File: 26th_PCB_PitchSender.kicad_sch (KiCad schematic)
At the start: 15 parts, among them J1 Amp, J2 Conn_01x04_Pin, J3 microSD, J4 Conn_01x04_Socket, J5 BNO055, J6 BMP390

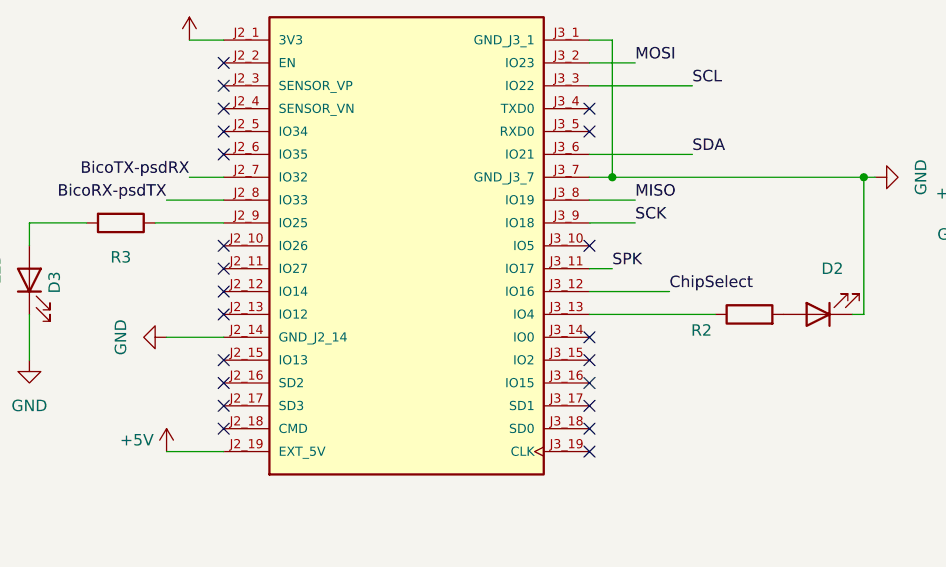
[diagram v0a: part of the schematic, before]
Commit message: Change SPK pin
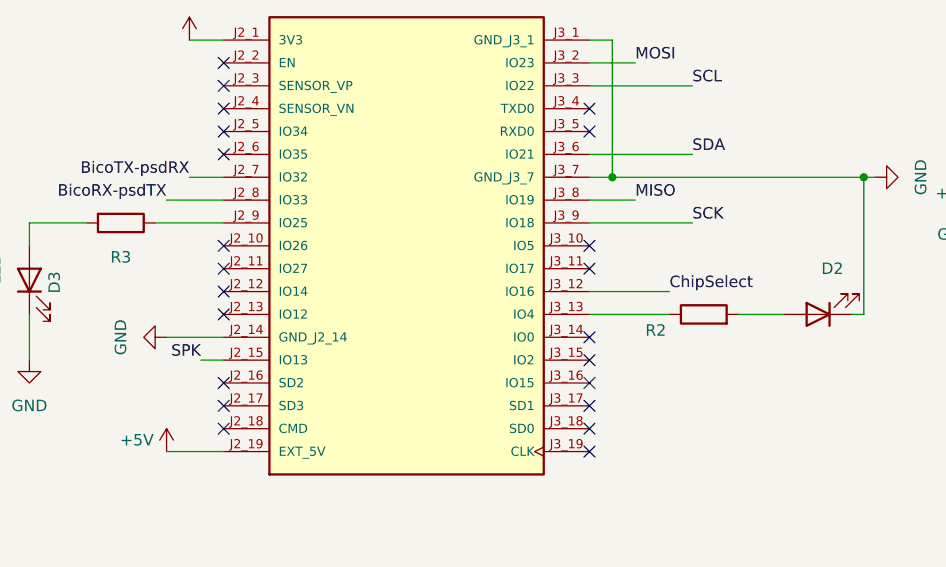
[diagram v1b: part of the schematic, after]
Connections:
- net SPK: now also U1.J2_15 (IO13); no longer U1.J3_11 (IO17)
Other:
- moved on the sheet: R2
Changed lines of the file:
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@@
 	)
 	(no_connect
-		(at 144.78 129.54)
-	)
-	(no_connect
 		(at 144.78 137.16)
 	)
@@
 	)
 	(no_connect
+		(at 185.42 119.38)
+	)
+	(no_connect
 		(at 144.78 121.92)
 	)
@@
 	(wire
 		(pts
-			(xy 185.42 119.38) (xy 187.96 119.38)
+			(xy 229.87 114.3) (xy 236.22 114.3)
 		)
 		(stroke
@@
 	(wire
 		(pts
-			(xy 229.87 114.3) (xy 236.22 114.3)
+			(xy 215.9 109.22) (xy 215.9 124.46)
 		)
 		(stroke
@@
 	(wire
 		(pts
-			(xy 215.9 109.22) (xy 215.9 124.46)
+			(xy 201.93 124.46) (xy 207.01 124.46)
 		)
 		(stroke
@@
 	(wire
 		(pts
-			(xy 185.42 114.3) (xy 190.5 114.3)
+			(xy 185.42 114.3) (xy 196.85 114.3)
 		)
 		(stroke
@@
 	(wire
 		(pts
+			(xy 142.24 129.54) (xy 144.78 129.54)
+		)
+		(stroke
+			(width 0)
+			(type default)
+		)
+	)
+	(wire
+		(pts
 			(xy 82.55 144.78) (xy 82.55 161.29)
 		)
@@
 	(wire
 		(pts
-			(xy 185.42 124.46) (xy 199.39 124.46)
+			(xy 185.42 124.46) (xy 194.31 124.46)
 		)
 		(stroke
@@
 		)
 	)
-	(label "SPK"
-		(at 187.96 119.38 0)
-		(effects
-			(font
-				(size 1.27 1.27)
-			)
-			(justify left bottom)
-		)
-	)
 	(label "SDA"
 		(at 196.85 106.68 0)
@@
 		)
 	)
+	(label "SPK"
+		(at 142.24 129.54 180)
+		(effects
+			(font
+				(size 1.27 1.27)
+			)
+			(justify right bottom)
+		)
+	)
 	(label "SCK"
-		(at 190.5 114.3 0)
+		(at 196.85 114.3 0)
 		(effects
 			(font
@@
 	(symbol
 		(lib_id "Device:R")
-		(at 203.2 124.46 90)
+		(at 198.12 124.46 90)
 		(unit 1)
 		(exclude_from_sim no)
@@
 		(dnp no)
 		(property "Reference" "R2"
-			(at 197.866 126.238 90)
+			(at 192.786 126.238 90)
 			(effects
 				(font
@@
 		)
 		(property "Value" "R"
-			(at 203.2 120.65 90)
+			(at 198.12 120.65 90)
 			(effects
 				(font
@@
 		)
 		(property "Footprint" "Resistor_THT:R_Axial_DIN0204_L3.6mm_D1.6mm_P5.08mm_Horizontal"
-			(at 203.2 126.238 90)
+			(at 198.12 126.238 90)
 			(effects
 				(font
@@
 		)
 		(property "Datasheet" "~"
-			(at 203.2 124.46 0)
+			(at 198.12 124.46 0)
 			(effects
 				(font
@@
 		)
 		(property "Description" "Resistor"
-			(at 203.2 124.46 0)
+			(at 198.12 124.46 0)
 			(effects
 				(font
